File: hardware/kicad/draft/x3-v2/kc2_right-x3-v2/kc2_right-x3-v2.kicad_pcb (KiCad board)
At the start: 2 copper layers, 163.7 x 122.5 mm, 94 parts, among them SW1 KEY_01, SW10 KEY_10, SW11 KEY_11, SW12 KEY_12, SW13 KEY_13, SW14 KEY_14, SW15 KEY_15, SW16 KEY_16, SW17 KEY_17, SW18 KEY_18, SW19 KEY_19, SW2 KEY_02, SW20 KEY_20, SW21 KEY_21, SW22 KEY_22, SW23 KEY_23, SW24 KEY_24, SW25 KEY_25, SW26 KEY_26, SW27 KEY_27, SW28 KEY_28, SW29 KEY_29, SW3 KEY_03, SW30 KEY_30, SW31 KEY_31, SW32 KEY_32, SW33 KEY_33, SW34 KEY_34, SW35 KEY_35, SW36 KEY_36, SW37 KEY_37, SW38 KEY_38, SW39 KEY_39, SW4 KEY_04, SW5 KEY_05, SW6 KEY_06, SW7 KEY_07, SW8 KEY_08, SW9 KEY_09, U1 nice!nano_v2_socket_24pin

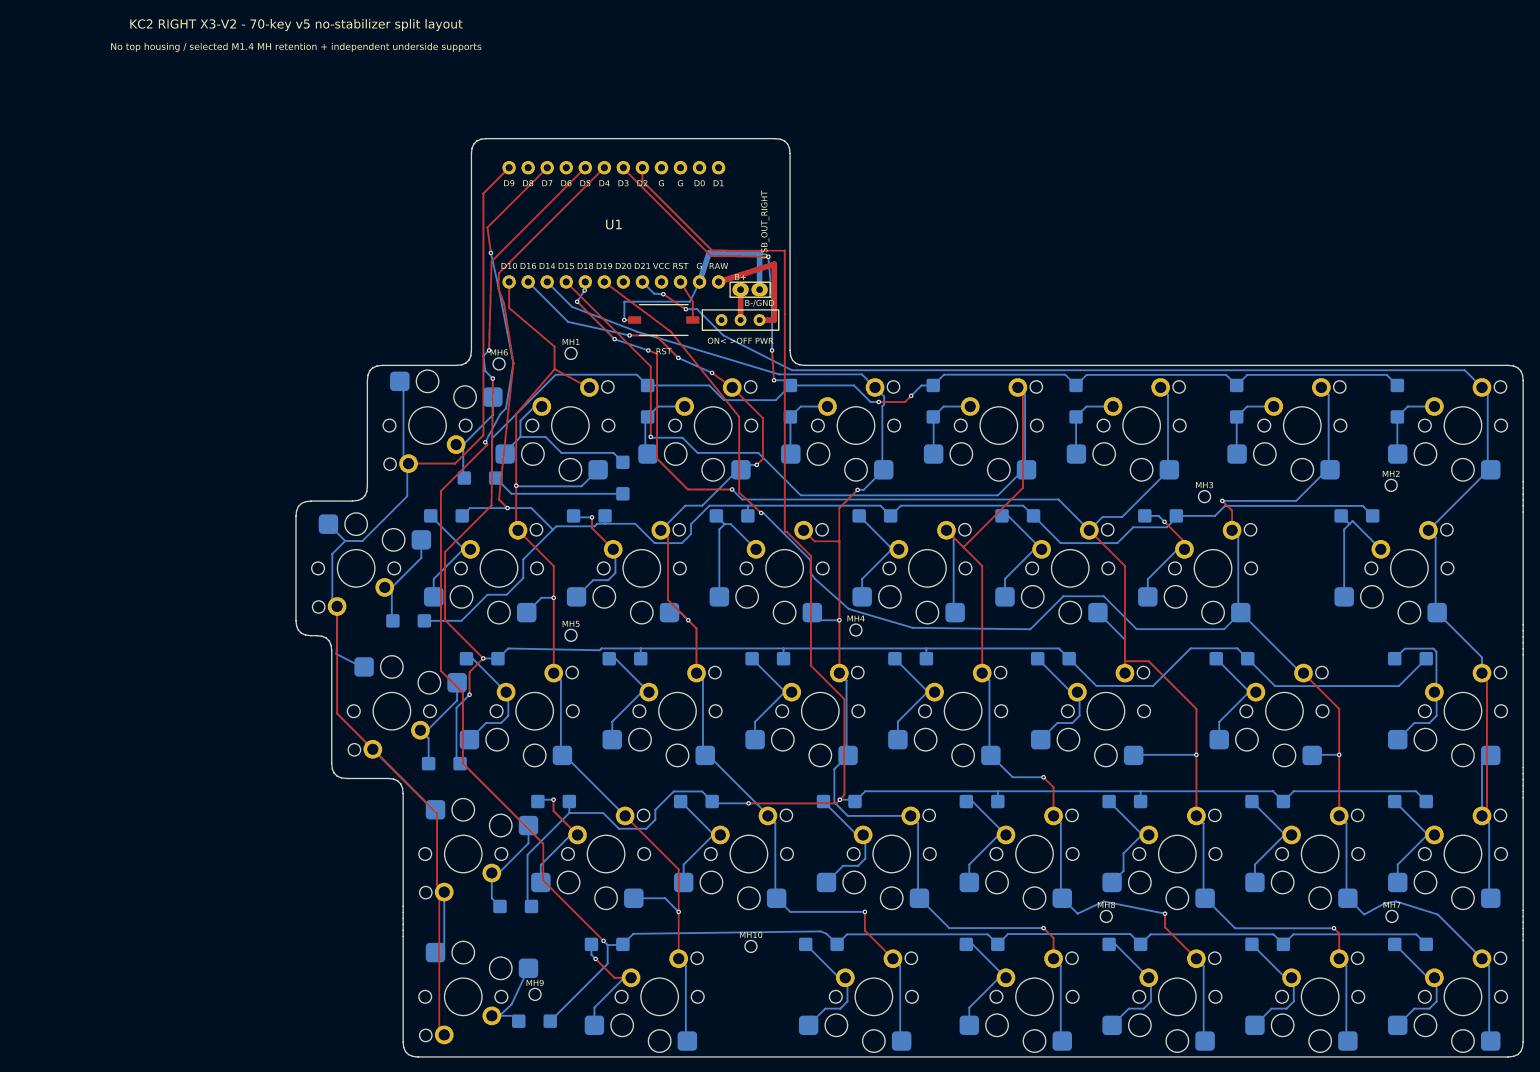
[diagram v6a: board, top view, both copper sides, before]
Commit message: wip(x3-v2): redesign mounts and per-key supports
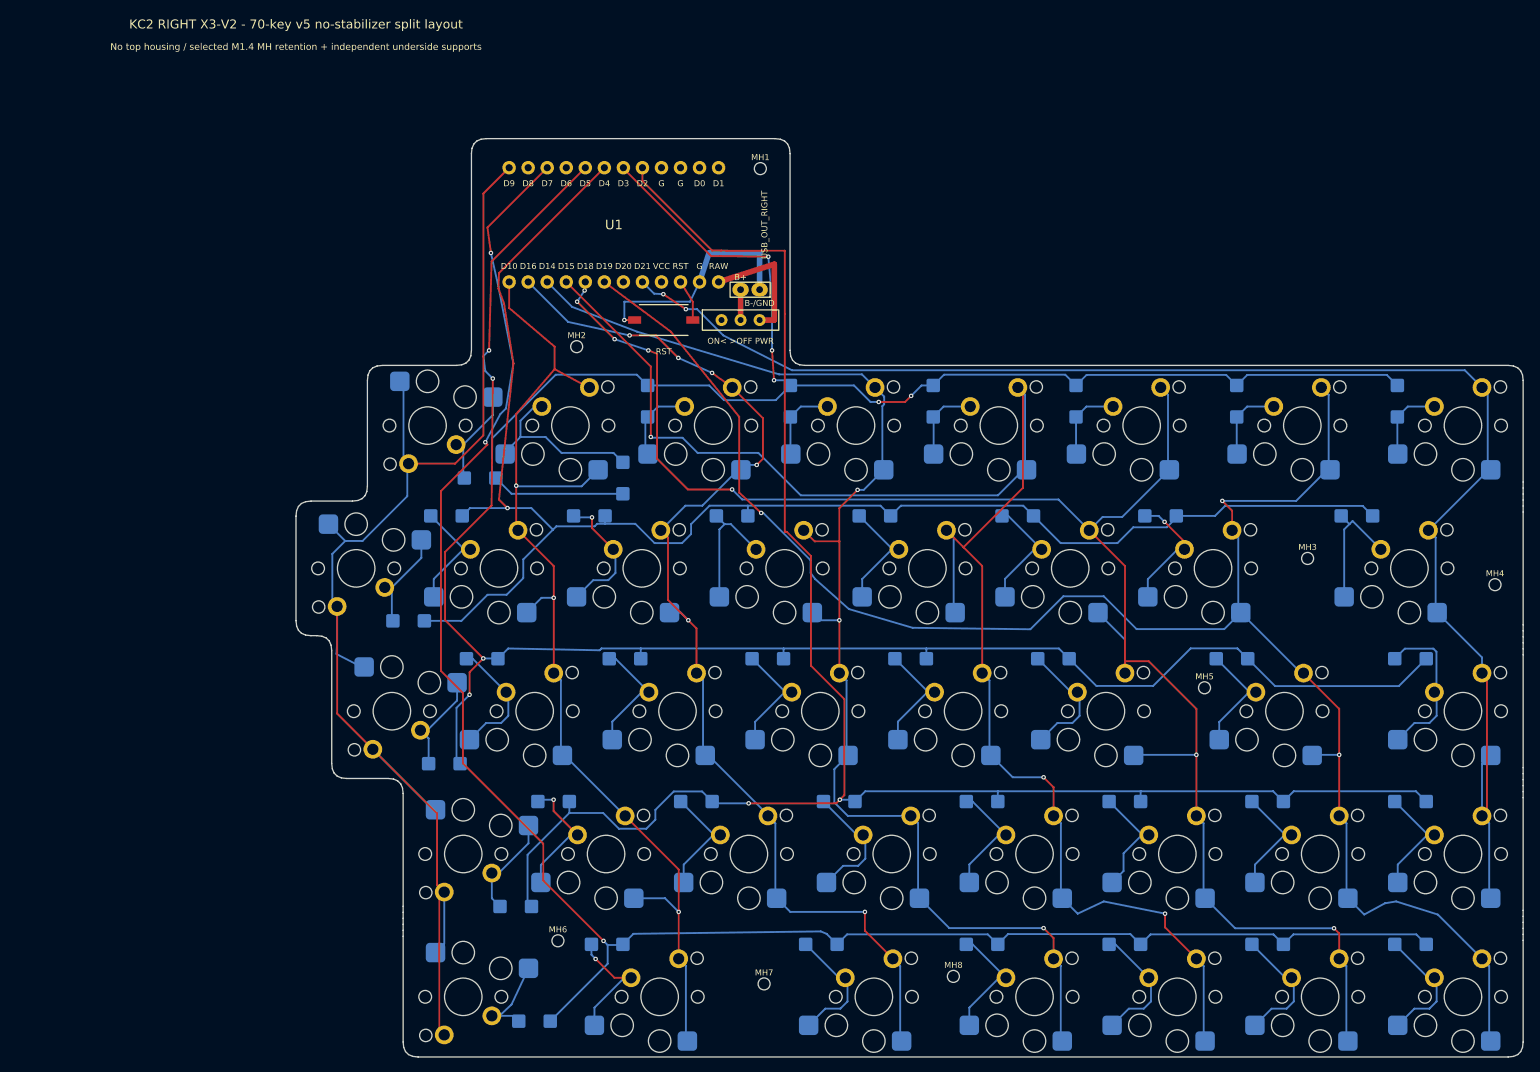
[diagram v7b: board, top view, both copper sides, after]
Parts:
- removed MH10, MH9: M1.4_NPTH_1.60, MH_M1.4_NPTH_1.60
- moved MH2 110.2 mm to (72.4, 67.0)
- moved MH4 85.5 mm to (194.9, 98.8)
- moved MH5 84.8 mm to (156.2, 112.5)
- moved MH7 84.2 mm to (97.4, 152.0)
- moved MH6 77.3 mm to (69.9, 146.2)
- moved MH1 35.3 mm to (96.9, 43.2)
- moved MH8 21.9 mm to (122.7, 151.0)
- moved MH3 16.0 mm to (169.9, 95.2)
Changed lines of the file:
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@@
 	(footprint "MH_M1.4_NPTH_1.60"
 		(layer "F.Cu")
-		(at 71.6875 105.5)
+		(at 156.1875 112.5)
 		(descr "KC2 X3 V2 M1.4 service mounting hole, 1.60 mm copper-free NPTH")
 		(tags "KC2 X3 V2 M1.4 mounting NPTH copper-free")
@@
 	(footprint "MH_M1.4_NPTH_1.60"
 		(layer "F.Cu")
-		(at 181.1875 143)
+		(at 97.4375 152)
 		(descr "KC2 X3 V2 M1.4 service mounting hole, 1.60 mm copper-free NPTH")
 		(tags "KC2 X3 V2 M1.4 mounting NPTH copper-free")
@@
 	(footprint "MH_M1.4_NPTH_1.60"
 		(layer "F.Cu")
-		(at 71.6875 67.9)
+		(at 96.9375 43.25)
 		(descr "KC2 X3 V2 M1.4 service mounting hole, 1.60 mm copper-free NPTH")
 		(tags "KC2 X3 V2 M1.4 mounting NPTH copper-free")
@@
 	(footprint "MH_M1.4_NPTH_1.60"
 		(layer "F.Cu")
-		(at 109.6875 104.8)
+		(at 194.9375 98.75)
 		(descr "KC2 X3 V2 M1.4 service mounting hole, 1.60 mm copper-free NPTH")
 		(tags "KC2 X3 V2 M1.4 mounting NPTH copper-free")
@@
 	(footprint "MH_M1.4_NPTH_1.60"
 		(layer "F.Cu")
-		(at 181.0875 85.5)
+		(at 72.4375 67)
 		(descr "KC2 X3 V2 M1.4 service mounting hole, 1.60 mm copper-free NPTH")
 		(tags "KC2 X3 V2 M1.4 mounting NPTH copper-free")
@@
 	(footprint "MH_M1.4_NPTH_1.60"
 		(layer "F.Cu")
-		(at 143.0875 143)
+		(at 122.6875 151)
 		(descr "KC2 X3 V2 M1.4 service mounting hole, 1.60 mm copper-free NPTH")
 		(tags "KC2 X3 V2 M1.4 mounting NPTH copper-free")
@@
 	(footprint "MH_M1.4_NPTH_1.60"
 		(layer "F.Cu")
-		(at 62.0875 69.3)
+		(at 69.9375 146.25)
 		(descr "KC2 X3 V2 M1.4 service mounting hole, 1.60 mm copper-free NPTH")
 		(tags "KC2 X3 V2 M1.4 mounting NPTH copper-free")
@@
 	(footprint "MH_M1.4_NPTH_1.60"
 		(layer "F.Cu")
-		(at 95.6875 147)
-		(descr "KC2 X3 V2 M1.4 service mounting hole, 1.60 mm copper-free NPTH")
-		(tags "KC2 X3 V2 M1.4 mounting NPTH copper-free")
-		(property "Reference" "MH10"
-			(at 0 -1.5 0)
-			(layer "F.SilkS")
-			(effects
-				(font
-					(size 0.8 0.8)
-					(thickness 0.15)
-				)
-			)
-		)
-		(property "Value" "M1.4_NPTH_1.60"
-			(at 0 0 0)
-			(layer "F.Fab")
-			(hide yes)
-			(effects
-				(font
-					(size 0.8 0.8)
-					(thickness 0.1)
-				)
-			)
-		)
-		(property "Datasheet" ""
-			(at 0 0 0)
-			(layer "F.Fab")
-			(hide yes)
-			(effects
-				(font
-					(size 1.27 1.27)
-				)
-			)
-		)
-		(property "Description" ""
-			(at 0 0 0)
-			(layer "F.Fab")
-			(hide yes)
-			(effects
-				(font
-					(size 1.27 1.27)
-				)
-			)
-		)
-		(attr exclude_from_pos_files exclude_from_bom)
-		(duplicate_pad_numbers_are_jumpers no)
-		(pad "" np_thru_hole circle
-			(at 0 0)
-			(size 1.6 1.6)
-			(drill 1.6)
-			(layers "*.Mask")
-		)
-		(embedded_fonts no)
-	)
-	(footprint "MH_M1.4_NPTH_1.60"
-		(layer "F.Cu")
-		(at 156.1875 87)
+		(at 169.9375 95.25)
 		(descr "KC2 X3 V2 M1.4 service mounting hole, 1.60 mm copper-free NPTH")
 		(tags "KC2 X3 V2 M1.4 mounting NPTH copper-free")
@@
 		)
 	)
-	(footprint "MH_M1.4_NPTH_1.60"
-		(layer "F.Cu")
-		(at 66.8875 153.4)
-		(descr "KC2 X3 V2 M1.4 service mounting hole, 1.60 mm copper-free NPTH")
-		(tags "KC2 X3 V2 M1.4 mounting NPTH copper-free")
-		(property "Reference" "MH9"
-			(at 0 -1.5 0)
-			(layer "F.SilkS")
-			(effects
-				(font
-					(size 0.8 0.8)
-					(thickness 0.15)
-				)
-			)
-		)
-		(property "Value" "M1.4_NPTH_1.60"
-			(at 0 0 0)
-			(layer "F.Fab")
-			(hide yes)
-			(effects
-				(font
-					(size 0.8 0.8)
-					(thickness 0.1)
-				)
-			)
-		)
-		(property "Datasheet" ""
-			(at 0 0 0)
-			(layer "F.Fab")
-			(hide yes)
-			(effects
-				(font
-					(size 1.27 1.27)
-				)
-			)
-		)
-		(property "Description" ""
-			(at 0 0 0)
-			(layer "F.Fab")
-			(hide yes)
-			(effects
-				(font
-					(size 1.27 1.27)
-				)
-			)
-		)
-		(attr exclude_from_pos_files exclude_from_bom)
-		(duplicate_pad_numbers_are_jumpers no)
-		(pad "" np_thru_hole circle
-			(at 0 0)
-			(size 1.6 1.6)
-			(drill 1.6)
-			(layers "*.Mask")
-		)
-		(embedded_fonts no)
-	)
 	(footprint "D_ES1B_SMA_HandSolder_C437840"

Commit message: wip(x3-v2): refresh P2 mounts and artifacts
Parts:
- moved MH1 0.12 mm to (97.1, 43.2)
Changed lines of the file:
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@@
 	(footprint "MH_M1.4_NPTH_1.60"
 		(layer "F.Cu")
-		(at 96.9375 43.25)
+		(at 97.0625 43.25)
 		(descr "KC2 X3 V2 M1.4 service mounting hole, 1.60 mm copper-free NPTH")
 		(tags "KC2 X3 V2 M1.4 mounting NPTH copper-free")
